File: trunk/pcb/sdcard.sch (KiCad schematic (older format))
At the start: 16 parts, among them P1 SDC_MMC_SOCKET, P2 CONN_8, Q1 MOSFET_P

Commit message: PCB V3.3 updated. Includes changes to SD card connector and interface board, which now includes the I2C Real Time Clock chip.
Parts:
- removed D1: LED, symbol LED
- removed L1: 10uH, symbol INDUCTOR
- removed Q1: MOSFET_P, symbol MOSFET_P
- removed R12: 10K, symbol R
- removed R4: 100, symbol R
- added BT1: CR2032, symbol BATTERY
- added C2: 0u1, symbol C
- added U1: DS1338-33, symbol DS1338-33
- added X1: 32768, symbol CRYSTAL
- C1: value C -> 0u1
- renumbered R5 to R4, R7 to R5, R8 to R6, R10 to R7, R11 to R8
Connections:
- net labels added: I2C_SCL, I2C_SDA
- net labels removed: SD_Pwr
- wire segments 57 -> 66
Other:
- note added: "Real Time Clock"
- moved on the sheet: C1, P1, P2, R1, R2, R3, R4, R5, R6, R7, R8

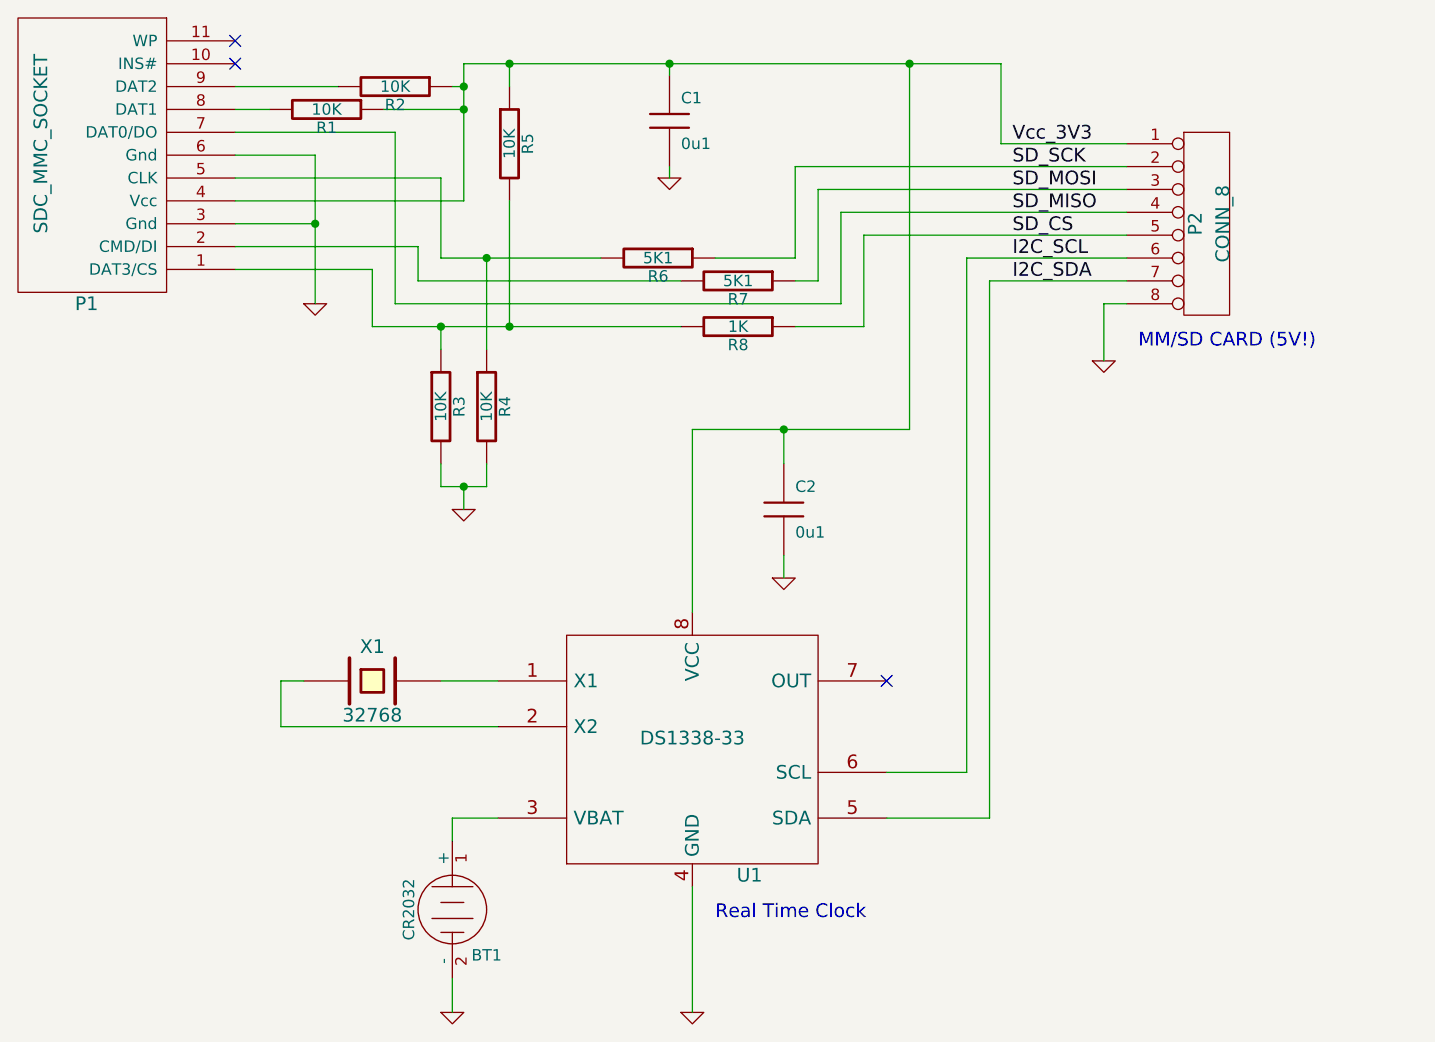
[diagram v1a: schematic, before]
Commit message: Oops. Forgot the I2C pull-up resistors on the SD card interface board.
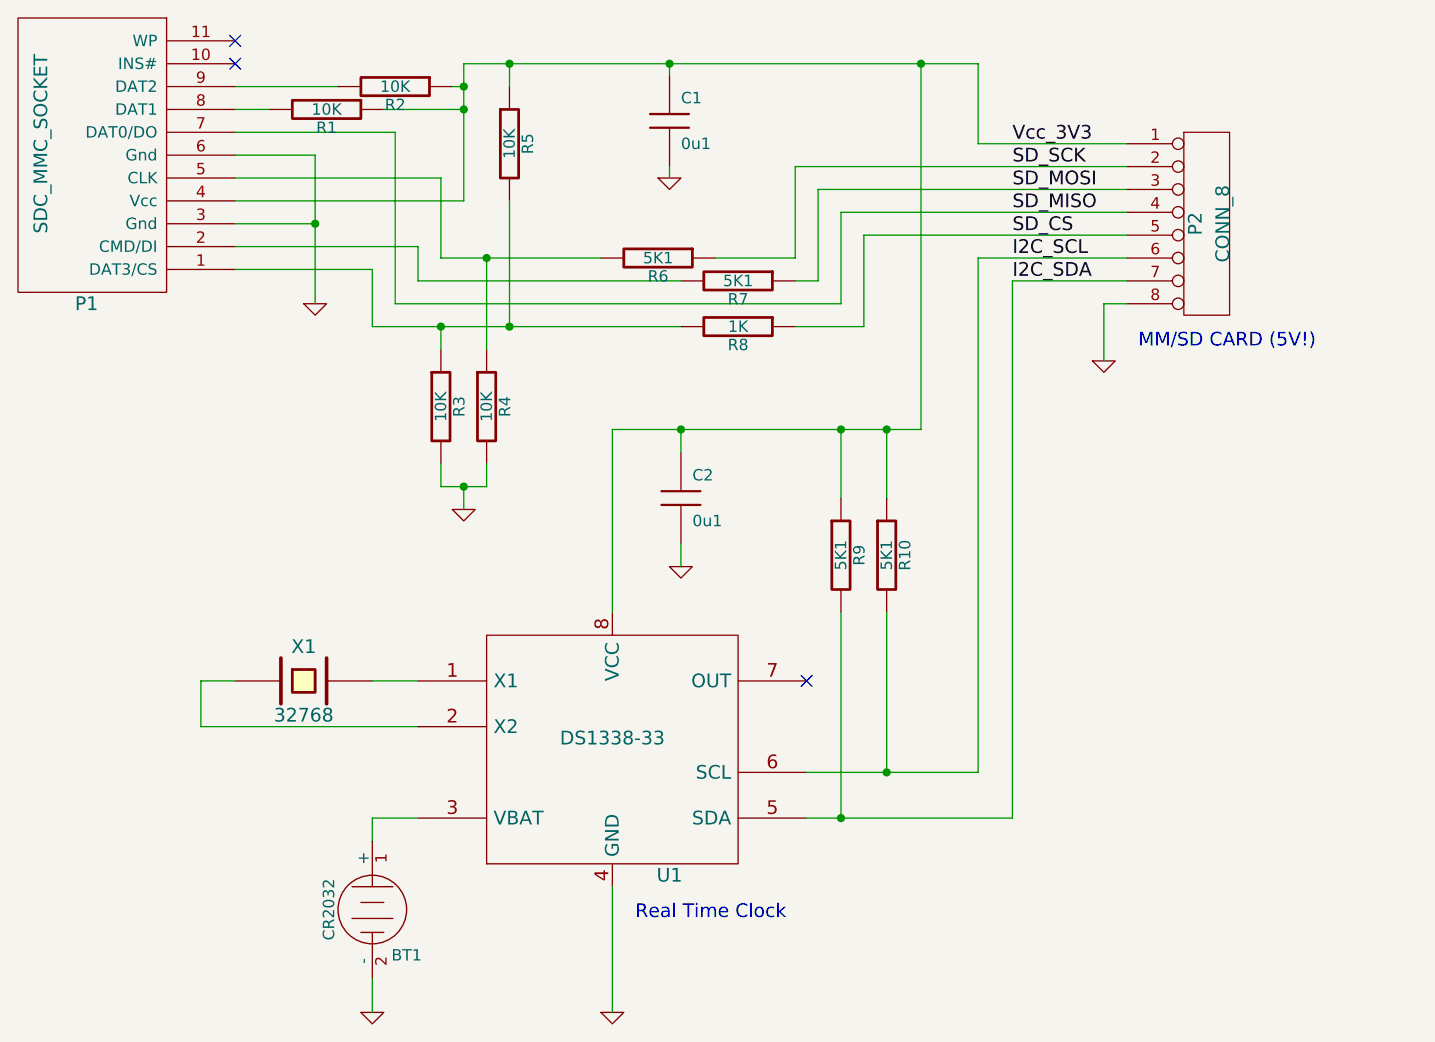
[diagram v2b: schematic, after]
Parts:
- added R10, R9: 5K1, symbol R
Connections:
- net I2C_SCL: now also R10.2
- net I2C_SDA: now also R9.2
- net Vcc_3V3: now also R10.1, R9.1
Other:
- moved on the sheet: BT1, C2, U1, X1
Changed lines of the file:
@@
-EESchema Schematic File Version 2  date 25/01/2011 4:16:10 p.m.
+EESchema Schematic File Version 2  date 25/01/2011 7:11:38 p.m.
 LIBS:power
 LIBS:device
@@
 Comment4 ""
 $EndDescr
+Connection ~ 6600 4800
+Wire Wire Line
+	6600 4100 6600 4800
+Connection ~ 6400 3300
+Wire Wire Line
+	6400 3600 6400 3300
 Wire Wire Line
 	5650 1700 5650 1750
 Wire Wire Line
-	6150 3950 6150 3850
-Wire Wire Line
-	5750 5850 5750 5300
-Wire Wire Line
-	4900 5000 4700 5000
-Wire Wire Line
-	4700 5000 4700 5100
-Wire Wire Line
-	4900 4400 4650 4400
-Wire Wire Line
-	7050 5000 7050 2650
-Wire Wire Line
-	7050 5000 6600 5000
-Wire Wire Line
-	4750 1700 7100 1700
-Wire Wire Line
-	4750 1700 4750 2300
+	5700 3900 5700 3800
+Wire Wire Line
+	5400 5850 5400 5300
+Wire Wire Line
+	4550 5000 4350 5000
+Wire Wire Line
+	4350 5000 4350 5100
+Wire Wire Line
+	4550 4400 4350 4400
+Wire Wire Line
+	7150 5000 7150 2650
+Wire Wire Line
+	7150 5000 6400 5000
+Wire Wire Line
+	6400 5000 6250 5000
+Wire Wire Line
+	4750 1700 4950 1700
+Wire Wire Line
+	4950 1700 5650 1700
+Wire Wire Line
+	5650 1700 6750 1700
+Wire Wire Line
+	6750 1700 7000 1700
+Wire Wire Line
+	4750 1700 4750 1800
+Wire Wire Line
+	4750 1800 4750 1900
+Wire Wire Line
+	4750 1900 4750 2300
 Wire Wire Line
 	7650 2450 6500 2450
@@
 	4350 2600 4350 2850
 Wire Wire Line
-	4350 2850 5700 2850
+	4350 2850 4650 2850
+Wire Wire Line
+	4650 2850 4950 2850
+Wire Wire Line
+	4950 2850 5700 2850
 Wire Wire Line
 	3750 2100 4100 2100
 Wire Wire Line
-	4100 2100 4100 2750
+	4100 2100 4100 2400
+Wire Wire Line
+	4100 2400 4100 2750
 Connection ~ 4850 2550
 Wire Wire Line
@@
 	4550 2650 5700 2650
 Wire Wire Line
-	7100 1700 7100 2050
+	7000 1700 7000 2050
 Wire Wire Line
 	7650 2750 7550 2750
@@
 	7550 2750 7550 3000
 Wire Wire Line
-	7100 2050 7650 2050
+	7000 2050 7650 2050
 Wire Wire Line
 	7650 2350 6400 2350
@@
 	6300 2250 7650 2250
 Wire Wire Line
-	5350 2550 4650 2550
+	5350 2550 4850 2550
+Wire Wire Line
+	4850 2550 4650 2550
 Wire Wire Line
 	4650 2550 4650 2200
@@
 	4450 2750 6400 2750
 Wire Wire Line
-	4650 3550 4850 3550
+	4650 3550 4750 3550
+Wire Wire Line
+	4750 3550 4850 3550
 Wire Wire Line
 	4850 3550 4850 3450
 Connection ~ 4750 3550
 Wire Wire Line
-	6600 4800 6950 4800
-Wire Wire Line
-	6950 4800 6950 2550
-Wire Wire Line
-	6950 2550 7650 2550
-Wire Wire Line
-	7050 2650 7650 2650
-Wire Wire Line
-	4050 4400 3950 4400
-Wire Wire Line
-	3950 4400 3950 4600
-Wire Wire Line
-	3950 4600 4900 4600
-Wire Wire Line
-	4700 5850 4700 5700
-Wire Wire Line
-	5750 4100 5750 3300
-Wire Wire Line
-	5750 3300 6700 3300
-Wire Wire Line
-	6700 3300 6700 1700
-Connection ~ 6700 1700
-Wire Wire Line
-	6150 3450 6150 3300
-Connection ~ 6150 3300
-Text Notes 5850 5450 0    60   ~ 0
+	6250 4800 6600 4800
+Wire Wire Line
+	6600 4800 7000 4800
+Wire Wire Line
+	7000 4800 7000 2550
+Wire Wire Line
+	7000 2550 7650 2550
+Wire Wire Line
+	7150 2650 7650 2650
+Wire Wire Line
+	3750 4400 3600 4400
+Wire Wire Line
+	3600 4400 3600 4600
+Wire Wire Line
+	3600 4600 4550 4600
+Wire Wire Line
+	4350 5850 4350 5700
+Wire Wire Line
+	5400 4100 5400 3300
+Wire Wire Line
+	5400 3300 5700 3300
+Wire Wire Line
+	5700 3300 6400 3300
+Wire Wire Line
+	6400 3300 6600 3300
+Wire Wire Line
+	6600 3300 6750 3300
+Wire Wire Line
+	6750 3300 6750 1700
+Connection ~ 6750 1700
+Wire Wire Line
+	5700 3400 5700 3300
+Connection ~ 5700 3300
+Wire Wire Line
+	6600 3600 6600 3300
+Connection ~ 6600 3300
+Wire Wire Line
+	6400 4100 6400 5000
+Connection ~ 6400 5000
+$Comp
+L R R10
+U 1 1 4D3E6931
+P 6600 3850
+F 0 "R10" V 6680 3850 50  0000 C CNN
+F 1 "5K1" V 6600 3850 50  0000 C CNN
+	1    6600 3850
+	1    0    0    -1
+$EndComp
+$Comp
+L R R9
+U 1 1 4D3E691F
+P 6400 3850
+F 0 "R9" V 6480 3850 50  0000 C CNN
+F 1 "5K1" V 6400 3850 50  0000 C CNN
+	1    6400 3850
+	1    0    0    -1
+$EndComp
+Text Notes 5500 5450 0    60   ~ 0
 Real Time Clock
 $Comp
 L GND #PWR6
 U 1 1 4D3E3F0B
-P 6150 3950
-F 0 "#PWR6" H 6150 3950 30  0001 C CNN
-F 1 "GND" H 6150 3880 30  0001 C CNN
-	1    6150 3950
+P 5700 3900
+F 0 "#PWR6" H 5700 3900 30  0001 C CNN
+F 1 "GND" H 5700 3830 30  0001 C CNN
+	1    5700 3900
 	1    0    0    -1
 $EndComp
@@
 L C C2
 U 1 1 4D3E3EFB
-P 6150 3650
-F 0 "C2" H 6200 3750 50  0000 L CNN
-F 1 "0u1" H 6200 3550 50  0000 L CNN
-	1    6150 3650
+P 5700 3600
+F 0 "C2" H 5750 3700 50  0000 L CNN
+F 1 "0u1" H 5750 3500 50  0000 L CNN
+	1    5700 3600
 	1    0    0    -1
 $EndComp
@@
 L GND #PWR2
 U 1 1 4D3E3EC2
-P 4700 5850
-F 0 "#PWR2" H 4700 5850 30  0001 C CNN
-F 1 "GND" H 4700 5780 30  0001 C CNN
-	1    4700 5850
-	1    0    0    -1
-$EndComp
-$Comp
-L GND #PWR5
+P 4350 5850
+F 0 "#PWR2" H 4350 5850 30  0001 C CNN
+F 1 "GND" H 4350 5780 30  0001 C CNN
+	1    4350 5850
+	1    0    0    -1
+$EndComp
+$Comp
+L GND #PWR4
 U 1 1 4D3E3EBC
-P 5750 5850
-F 0 "#PWR5" H 5750 5850 30  0001 C CNN
-F 1 "GND" H 5750 5780 30  0001 C CNN
-	1    5750 5850
+P 5400 5850
+F 0 "#PWR4" H 5400 5850 30  0001 C CNN
+F 1 "GND" H 5400 5780 30  0001 C CNN
+	1    5400 5850
 	1    0    0    -1
 $EndComp
@@
 L BATTERY BT1
 U 1 1 4D3E3E91
-P 4700 5400
-F 0 "BT1" V 4900 5550 50  0000 C CNN
-F 1 "CR2032" H 4700 5210 50  0000 C CNN
-	1    4700 5400
+P 4350 5400
+F 0 "BT1" V 4550 5550 50  0000 C CNN
+F 1 "CR2032" H 4350 5210 50  0000 C CNN
+	1    4350 5400
 	0    1    1    0
 $EndComp
@@
 L CRYSTAL X1
 U 1 1 4D3E3E59
-P 4350 4400
-F 0 "X1" H 4350 4550 60  0000 C CNN
-F 1 "32768" H 4350 4250 60  0000 C CNN
-	1    4350 4400
-	1    0    0    -1
-$EndComp
-NoConn ~ 6600 4400
+P 4050 4400
+F 0 "X1" H 4050 4550 60  0000 C CNN
+F 1 "32768" H 4050 4250 60  0000 C CNN
+	1    4050 4400
+	1    0    0    -1
+$EndComp
+NoConn ~ 6250 4400
 $Comp
 L DS1338-33 U1
 U 1 1 4D3E3DEA
-P 5750 4700
-F 0 "U1" H 6000 4150 60  0000 C CNN
-F 1 "DS1338-33" H 5750 4750 60  0000 C CNN
-	1    5750 4700
+P 5400 4700
+F 0 "U1" H 5650 4150 60  0000 C CNN
+F 1 "DS1338-33" H 5400 4750 60  0000 C CNN
+	1    5400 4700
 	1    0    0    -1
 $EndComp
@@
 $EndComp
 $Comp
-L GND #PWR4
+L GND #PWR5
 U 1 1 4D1F9457
 P 5650 2200
-F 0 "#PWR4" H 5650 2200 30  0001 C CNN
+F 0 "#PWR5" H 5650 2200 30  0001 C CNN
 F 1 "GND" H 5650 2130 30  0001 C CNN
 	1    5650 2200
